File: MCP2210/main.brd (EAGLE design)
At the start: 160 x 100 mm, 1 part, among them J1 USB_A_SMT_MALE

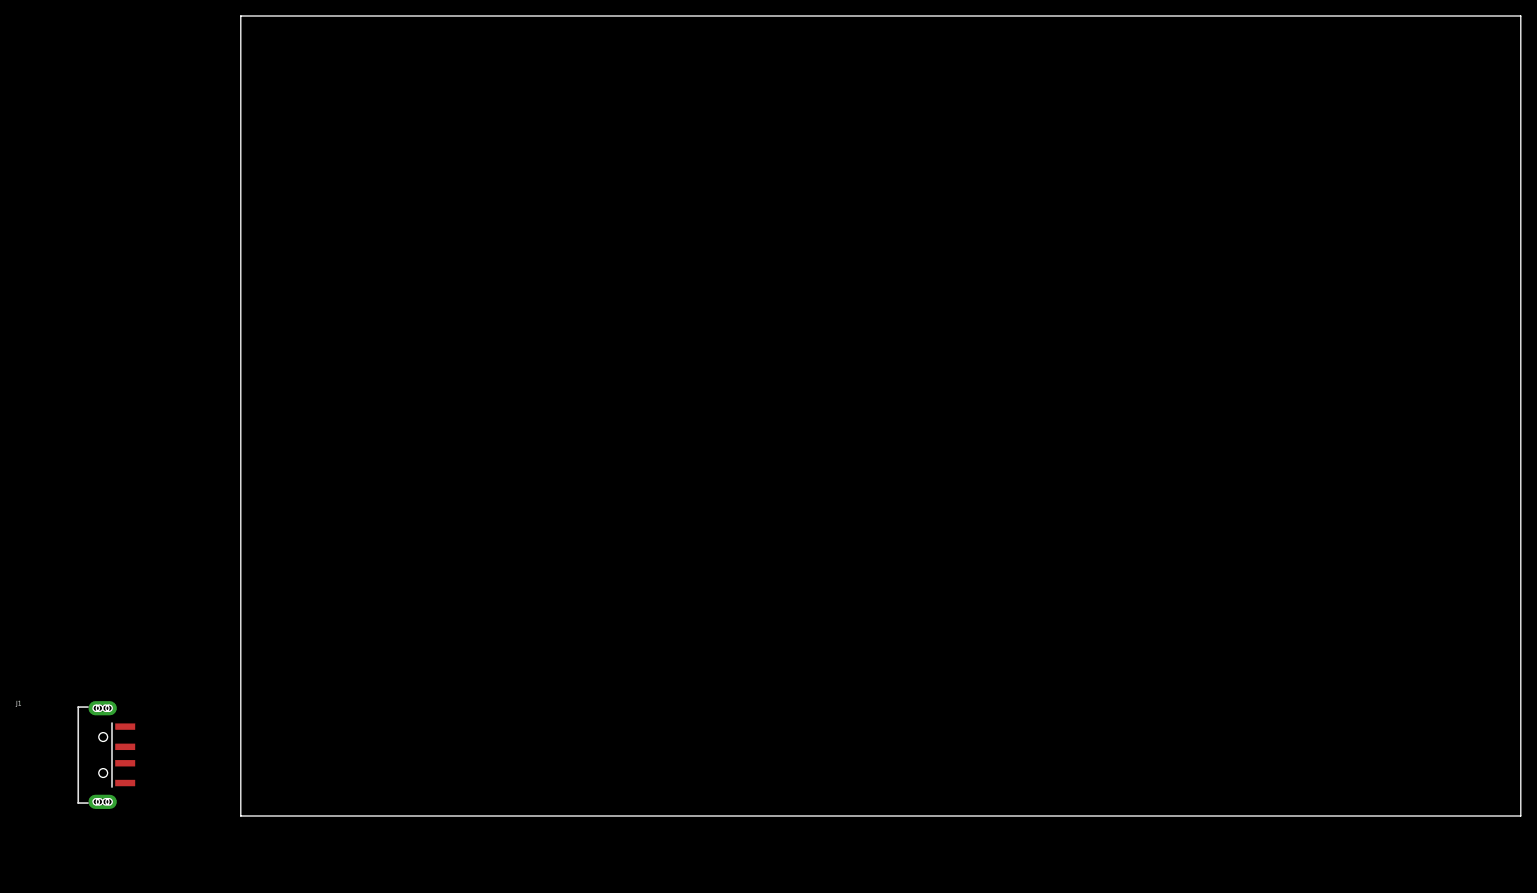
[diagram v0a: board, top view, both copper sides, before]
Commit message: resized outline
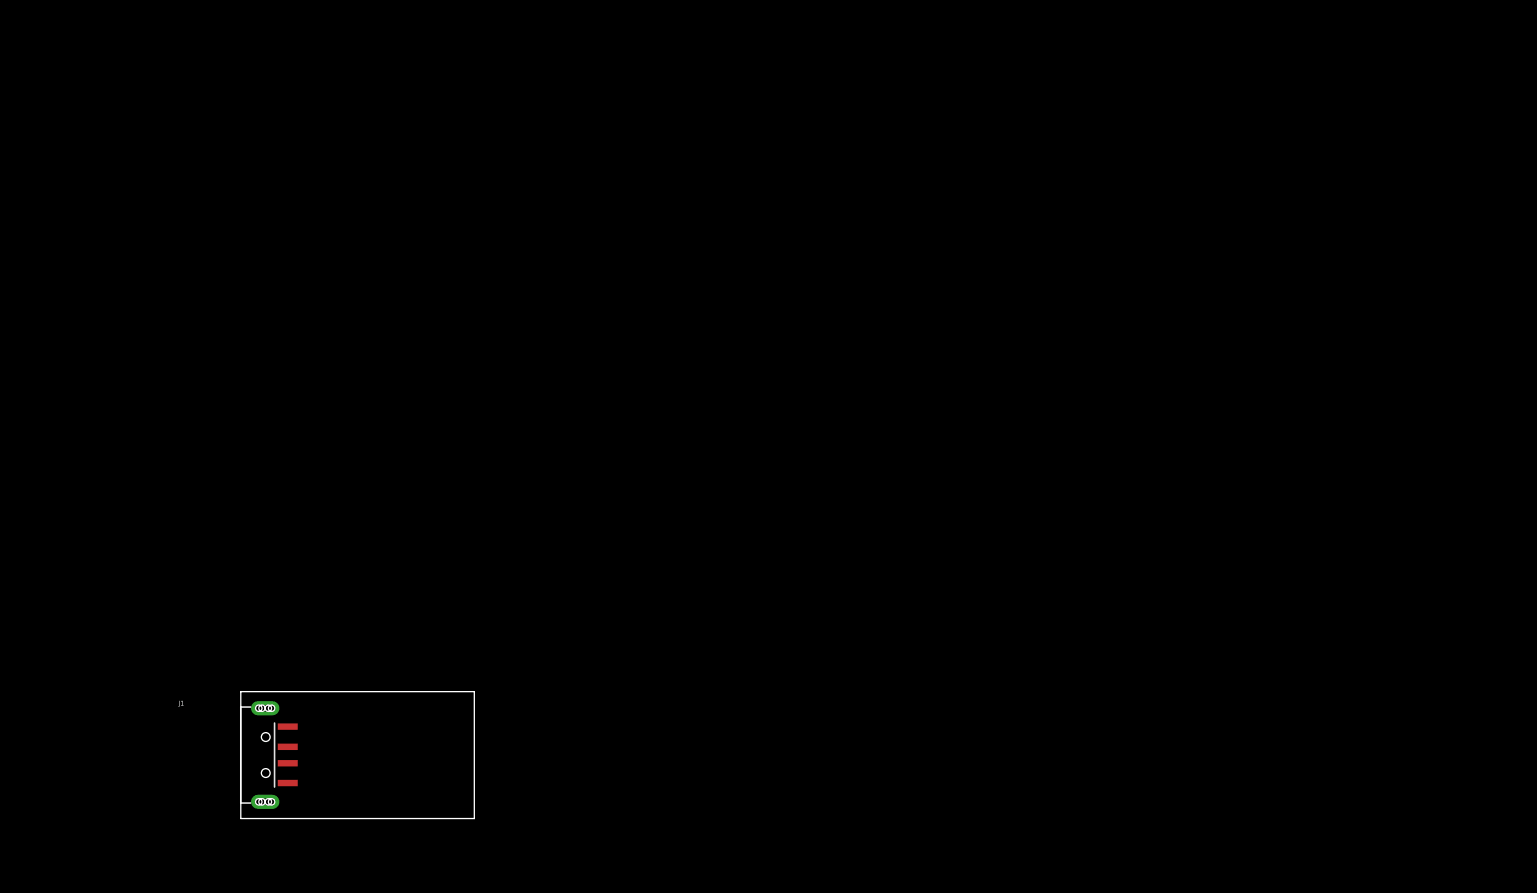
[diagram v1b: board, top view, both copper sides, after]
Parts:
- moved J1 20.3 mm to (-5.08, 7.62)
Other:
- board size 160 x 100 mm -> 29.2 x 15.9 mm
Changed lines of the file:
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@@
 <setting verticaltext="up"/>
 </settings>
-<grid distance="50" unitdist="mil" unit="mil" style="lines" multiple="1" display="no" altdistance="5" altunitdist="mil" altunit="mil"/>
+<grid distance="12.5" unitdist="mil" unit="mil" style="dots" multiple="1" display="yes" altdistance="5" altunitdist="mil" altunit="mil"/>
 <layers>
 <layer number="1" name="Top" color="4" fill="1" visible="yes" active="yes"/>
@@
 <board>
 <plain>
-<wire x1="0" y1="0" x2="160" y2="0" width="0" layer="20"/>
-<wire x1="160" y1="0" x2="160" y2="100" width="0" layer="20"/>
-<wire x1="160" y1="100" x2="0" y2="100" width="0" layer="20"/>
-<wire x1="0" y1="100" x2="0" y2="0" width="0" layer="20"/>
+<wire x1="0" y1="-0.3175" x2="29.19" y2="-0.3175" width="0" layer="20"/>
+<wire x1="29.19" y1="-0.3175" x2="29.19" y2="15.545" width="0" layer="20"/>
+<wire x1="29.19" y1="15.545" x2="0" y2="15.545" width="0" layer="20"/>
+<wire x1="0" y1="15.545" x2="0" y2="-0.3175" width="0" layer="20"/>
 </plain>
 <attributes>
@@
 </autorouter>
 <elements>
-<element name="J1" library="SparkFun-Connectors" library_urn="urn:adsk.eagle:library:513" package="USB-A-SMT-MALE" package3d_urn="urn:adsk.eagle:package:38305/1" value="USB_A_SMT_MALE" x="-25.4" y="7.62">
-<attribute name="NAME" x="-28.1" y="13.79" size="0.6096" layer="25" font="vector" ratio="20"/>
-<attribute name="PROD_ID" value="CONN-11499" x="0" y="0" size="1.778" layer="27" display="off"/>
+<element name="J1" library="SparkFun-Connectors" library_urn="urn:adsk.eagle:library:513" package="USB-A-SMT-MALE" package3d_urn="urn:adsk.eagle:package:38305/1" value="USB_A_SMT_MALE" x="-5.08" y="7.62">
+<attribute name="NAME" x="-7.78" y="13.79" size="0.6096" layer="25" font="vector" ratio="20"/>
+<attribute name="PROD_ID" value="CONN-11499" x="20.32" y="0" size="1.778" layer="27" display="off"/>
 </element>
 </elements>

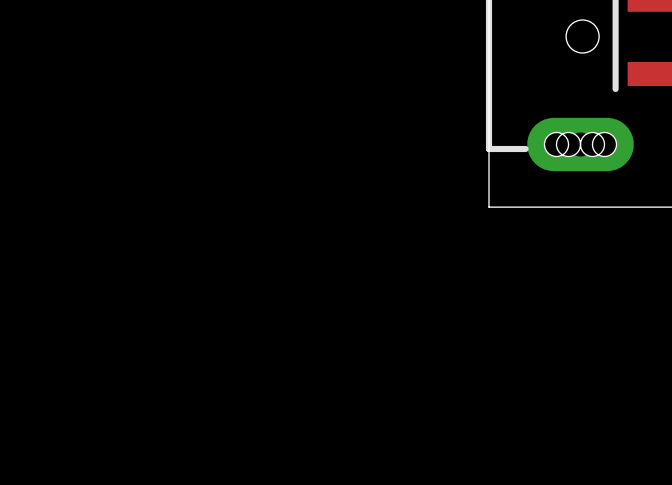
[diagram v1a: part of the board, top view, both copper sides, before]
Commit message: added crystal
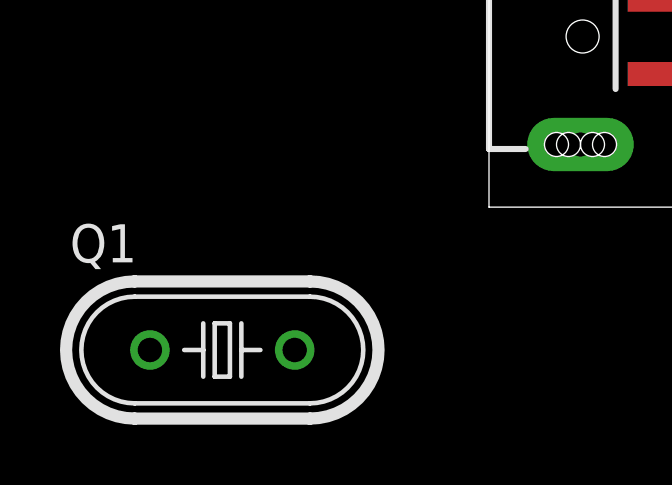
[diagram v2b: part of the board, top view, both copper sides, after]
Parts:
- added Q1: (no value), crystal:HC49U-V
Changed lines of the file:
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@@
 <attribute name="PROD_ID" value="CONN-11499" x="20.32" y="0" size="1.778" layer="27" display="off"/>
+</element>
+<element name="Q1" library="crystal" library_urn="urn:adsk.eagle:library:204" package="HC49U-V" package3d_urn="urn:adsk.eagle:package:12075/1" value="" x="-8.89" y="-5.08">
+<attribute name="MF" value="" x="-8.89" y="-5.08" size="1.778" layer="27" display="off"/>
+<attribute name="MPN" value="" x="-8.89" y="-5.08" size="1.778" layer="27" display="off"/>
+<attribute name="NAME" x="-13.97" y="-2.159" size="1.27" layer="25" ratio="10"/>
+<attribute name="OC_FARNELL" value="1666969" x="-8.89" y="-5.08" size="1.778" layer="27" display="off"/>
+<attribute name="OC_NEWARK" value="unknown" x="-8.89" y="-5.08" size="1.778" layer="27" display="off"/>
+<attribute name="VALUE" x="-13.97" y="-9.271" size="1.27" layer="27" ratio="10"/>
 </element>
 </elements>

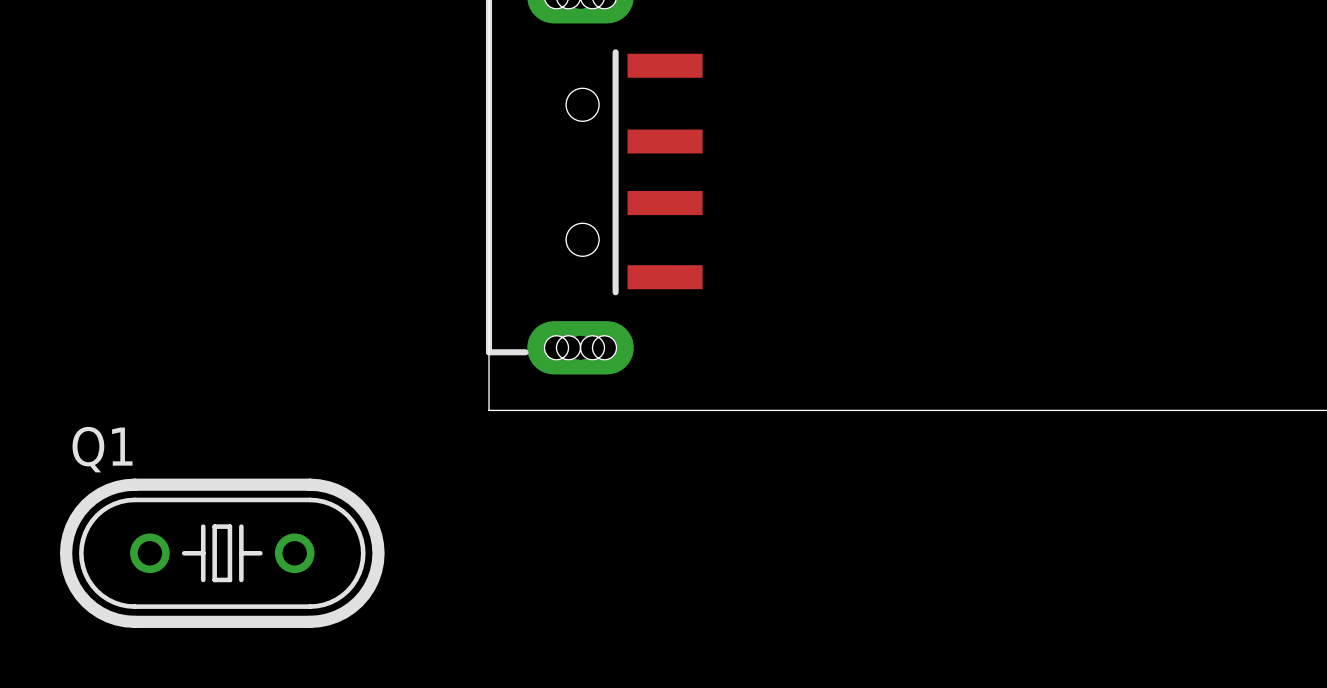
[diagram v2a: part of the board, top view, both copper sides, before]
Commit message: added crystal
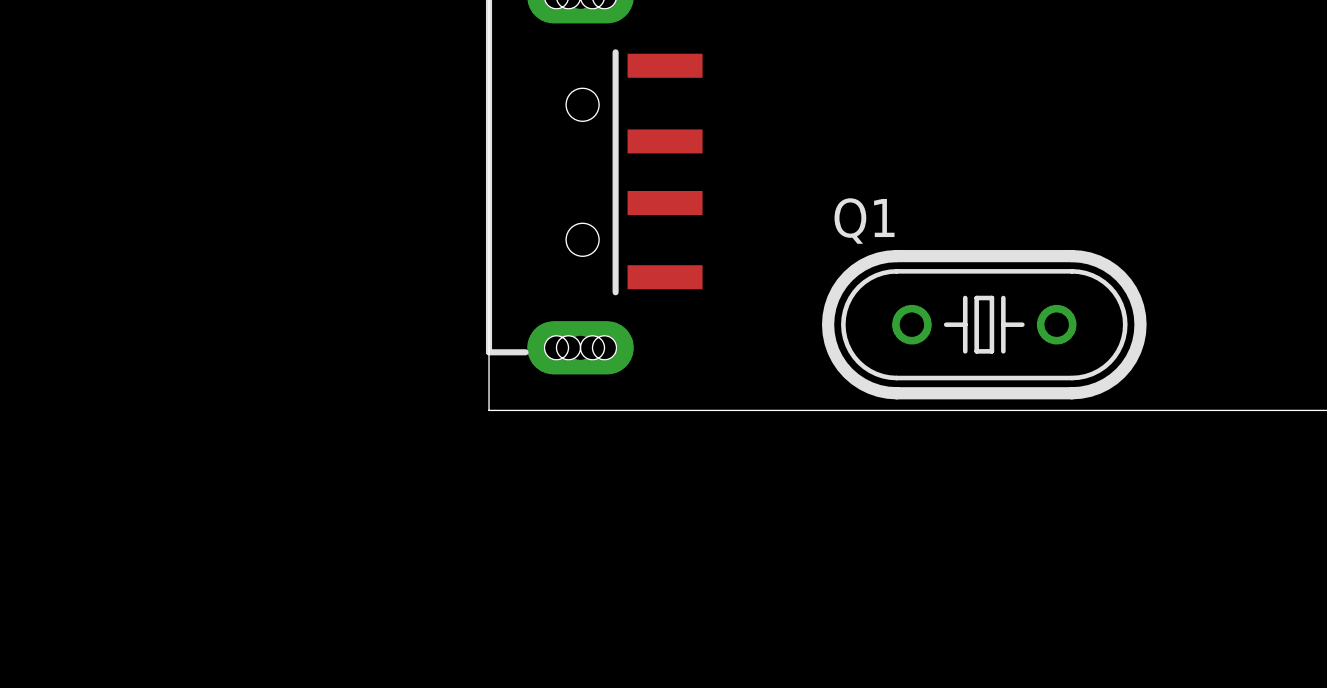
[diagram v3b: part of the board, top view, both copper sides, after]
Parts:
- moved Q1 26.5 mm to (16.5, 2.54)
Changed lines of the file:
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@@
 <attribute name="PROD_ID" value="CONN-11499" x="20.32" y="0" size="1.778" layer="27" display="off"/>
 </element>
-<element name="Q1" library="crystal" library_urn="urn:adsk.eagle:library:204" package="HC49U-V" package3d_urn="urn:adsk.eagle:package:12075/1" value="" x="-8.89" y="-5.08">
-<attribute name="MF" value="" x="-8.89" y="-5.08" size="1.778" layer="27" display="off"/>
-<attribute name="MPN" value="" x="-8.89" y="-5.08" size="1.778" layer="27" display="off"/>
-<attribute name="NAME" x="-13.97" y="-2.159" size="1.27" layer="25" ratio="10"/>
-<attribute name="OC_FARNELL" value="1666969" x="-8.89" y="-5.08" size="1.778" layer="27" display="off"/>
-<attribute name="OC_NEWARK" value="unknown" x="-8.89" y="-5.08" size="1.778" layer="27" display="off"/>
-<attribute name="VALUE" x="-13.97" y="-9.271" size="1.27" layer="27" ratio="10"/>
+<element name="Q1" library="crystal" library_urn="urn:adsk.eagle:library:204" package="HC49U-V" package3d_urn="urn:adsk.eagle:package:12075/1" value="" x="16.51" y="2.54">
+<attribute name="MF" value="" x="16.51" y="2.54" size="1.778" layer="27" display="off"/>
+<attribute name="MPN" value="" x="16.51" y="2.54" size="1.778" layer="27" display="off"/>
+<attribute name="NAME" x="11.43" y="5.461" size="1.27" layer="25" ratio="10"/>
+<attribute name="OC_FARNELL" value="1666969" x="16.51" y="2.54" size="1.778" layer="27" display="off"/>
+<attribute name="OC_NEWARK" value="unknown" x="16.51" y="2.54" size="1.778" layer="27" display="off"/>
+<attribute name="VALUE" x="11.43" y="-1.651" size="1.27" layer="27" ratio="10"/>
 </element>
 </elements>
